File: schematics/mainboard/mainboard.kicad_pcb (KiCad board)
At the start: 4 copper layers, 99.5 x 193.5 mm, 94 parts, among them J1 SD_Card_Receptacle, J2 LCD_CONN, J3 USB_C_Receptacle_USB2.0_16P, J4 BATTERY_CONN, J5 527461671, J7 SPEAKER, J9 AudioJack3, P1 1-1473005-4, SW1 SW_SPST, U1 AMS1117-3.3, U2 AMS1117-3.3, U3 MAX3421EETJ_T, U5 AMS1117-1.8, U6 TPS63002, U7 BQ24072RGT, Y1 12MHz

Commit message: Added load switch to mainboard to control startup.
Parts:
- added C39: 47uF, Capacitor_SMD:CP_Elec_5x5.3, F.Cu at (125.8, 114.4)
- added C41: 200pF, Capacitor_SMD:C_0805_2012Metric, F.Cu at (152.2, 259.6)
- added R32: ~, Resistor_SMD:R_0603_1608Metric_Pad0.98x0.95mm_HandSolder, F.Cu at (152.2, 255.8)
- added U9: TPS22917DBV, Package_TO_SOT_SMD:SOT-23-6, F.Cu at (148.2, 257.6)
- moved C4 6.12 mm to (120.0, 112.8)
- moved R29 6.12 mm to (120.0, 115.3)
- moved R7 1.35 mm to (165.8, 268.9)
- moved R6 1.25 mm to (172.4, 268.9)
- moved R2 0.15 mm to (168.0, 268.9)
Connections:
- SW1 pad 2: SYS_LOAD -> Net-(SW1-B)
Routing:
- net Net-(J3-CC1): track 6.84 -> 5.31 mm
- net Net-(J3-CC2): track 6.64 -> 5.39 mm
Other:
- board text added: "3V3 (LCD, SD, AUDIO)"

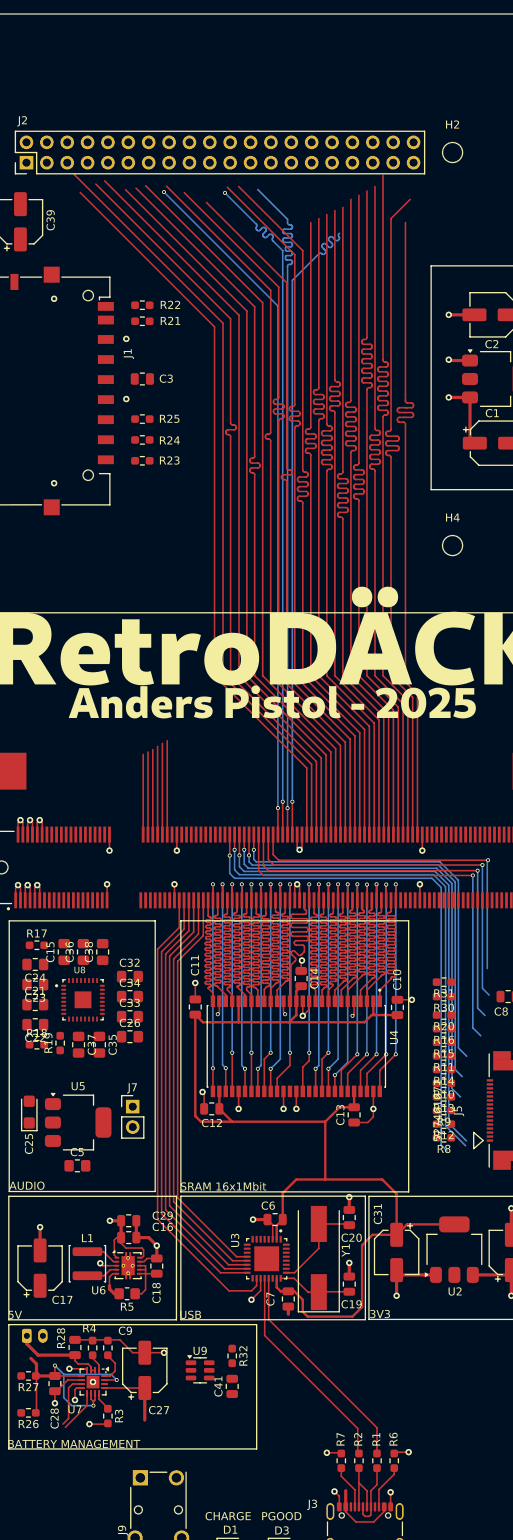
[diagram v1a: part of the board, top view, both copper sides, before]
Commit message: Mounting points for mainboard added. Adjusted position of track ball on buttboard.
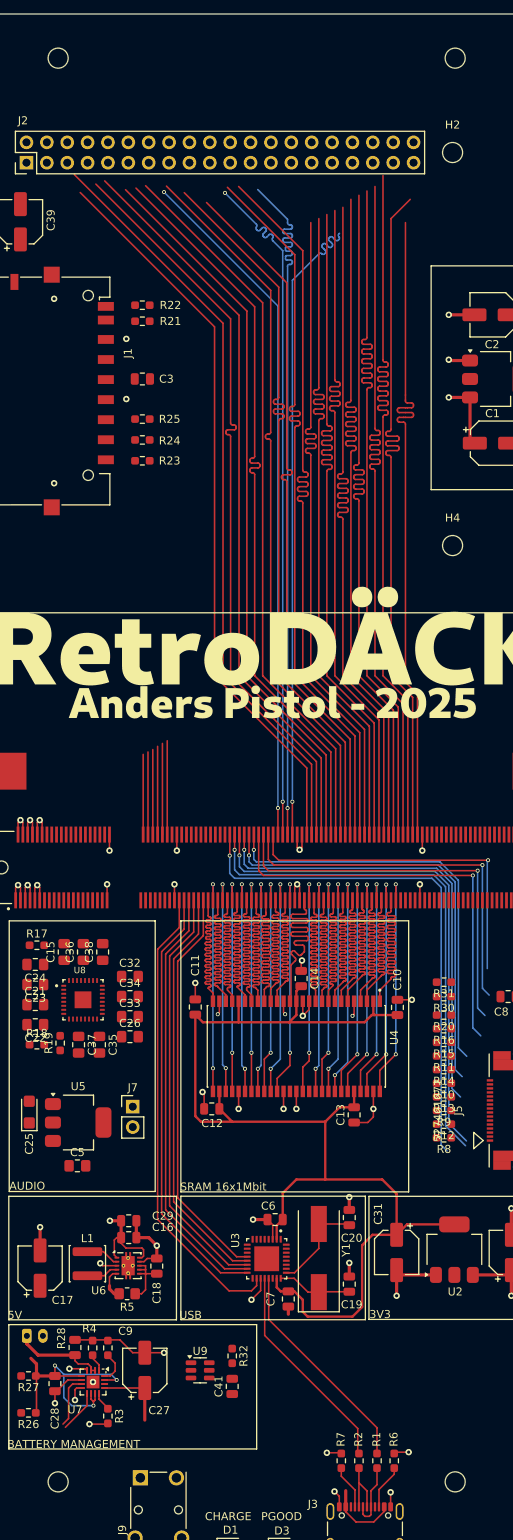
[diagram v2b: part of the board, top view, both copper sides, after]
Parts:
- added H5: MountingHole, MountingHole:MountingHole_2.5mm, F.Cu at (130.5, 94.0)
- added H6: MountingHole, MountingHole:MountingHole_2.5mm, F.Cu at (180.0, 94.0)
- added H7: MountingHole, MountingHole:MountingHole_2.5mm, F.Cu at (130.5, 271.5)
- added H8: MountingHole, MountingHole:MountingHole_2.5mm, F.Cu at (180.0, 271.5)

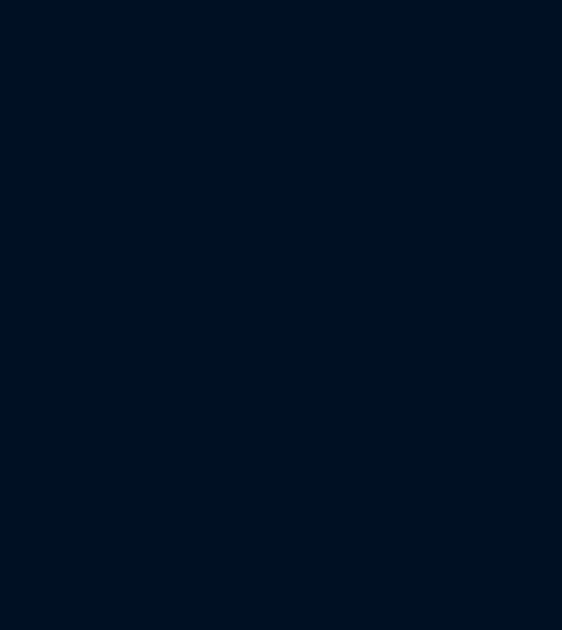
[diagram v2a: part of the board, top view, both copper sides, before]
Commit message: Schematic work; I2C shared with trackball and audio chip.
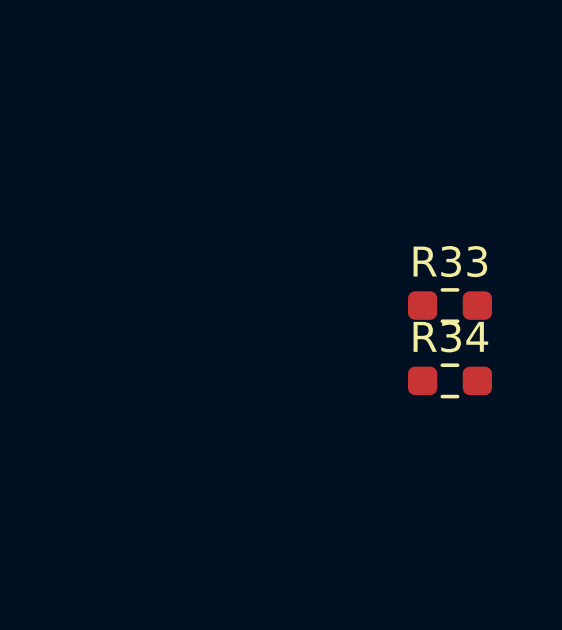
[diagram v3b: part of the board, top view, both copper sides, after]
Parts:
- added R33: 4k7, Resistor_SMD:R_0603_1608Metric_Pad0.98x0.95mm_HandSolder, F.Cu at (238.0, 211.5)
- added R34: 4k7, Resistor_SMD:R_0603_1608Metric_Pad0.98x0.95mm_HandSolder, F.Cu at (238.0, 214.0)
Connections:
- P1 pad 54: unconnected-(P1-Pad54) -> SD_CARD
- P1 pad 64: unconnected-(P1-Pad64) -> AUDIO_DIN
- P1 pad 66: unconnected-(P1-Pad66) -> AUDIO_WCLK
- P1 pad 68: unconnected-(P1-Pad68) -> AUDIO_BCLK
- P1 pad 70: unconnected-(P1-Pad70) -> AUDIO_MCLK
- U8 pad 10: AUDIO_SCL -> I2C_SCL
- U8 pad 9: AUDIO_SDA -> I2C_SDA

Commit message: Some work on the mainboard.
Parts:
- removed J7: SPEAKER, Connector_PinHeader_2.54mm:PinHeader_1x02_P2.54mm_Vertical
- removed R18, R19: 4k7, Resistor_SMD:R_0603_1608Metric_Pad0.98x0.95mm_HandSolder
- removed R30, R31: 1k2, Resistor_SMD:R_0603_1608Metric_Pad0.98x0.95mm_HandSolder
- added C40: 47uF, Capacitor_SMD:CP_Elec_5x5.3, F.Cu at (184.6, 118.9)
- added J6: SPEAKER_CONN, Connector_JST:JST_PH_S2B-PH-K_1x02_P2.00mm_Horizontal, F.Cu at (119.0, 224.0)
- moved C4 3.00 mm to (117.0, 112.8)
- moved C39 2.91 mm to (122.9, 114.2), turned to -90 degrees
- moved R29 2.12 mm to (118.0, 116.0), turned to 90 degrees
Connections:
- net I2C_INTERRUPT renamed TRACKBALL_INTERRUPT
- P1 pad 72: unconnected-(P1-Pad72) -> AUDIO_INTERRUPT
- U8 pad 32: GPIO1 -> AUDIO_INTERRUPT
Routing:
- net GND: track 146.2 -> 205.9 mm, vias 54 -> 55
- net 3V3_AUDIO: track 8.64 -> 67.5 mm
- net USB_VBUS: track 18.1 -> 47.5 mm
- net LCD_R4: track 88.1 -> 58.9 mm
- net LCD_B2: track 91.7 -> 71.8 mm
- net SD_CARD: track 0.00 -> 18.3 mm
- net LCD_B4: track 84.2 -> 71.5 mm
- net LCD_B3: track 85.6 -> 97.6 mm
- net LCD_ENABLE: track 86.3 -> 97.1 mm
- net 1V8: track 0.00 -> 8.72 mm
- net LCD_CLK: track 89.2 -> 97.5 mm
- net LCD_B1: track 89.8 -> 96.9 mm
- net LCD_G3: track 90.8 -> 97.6 mm
- net LCD_R5: track 91.4 -> 97.9 mm
- net LCD_CS: track 90.7 -> 97.0 mm
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
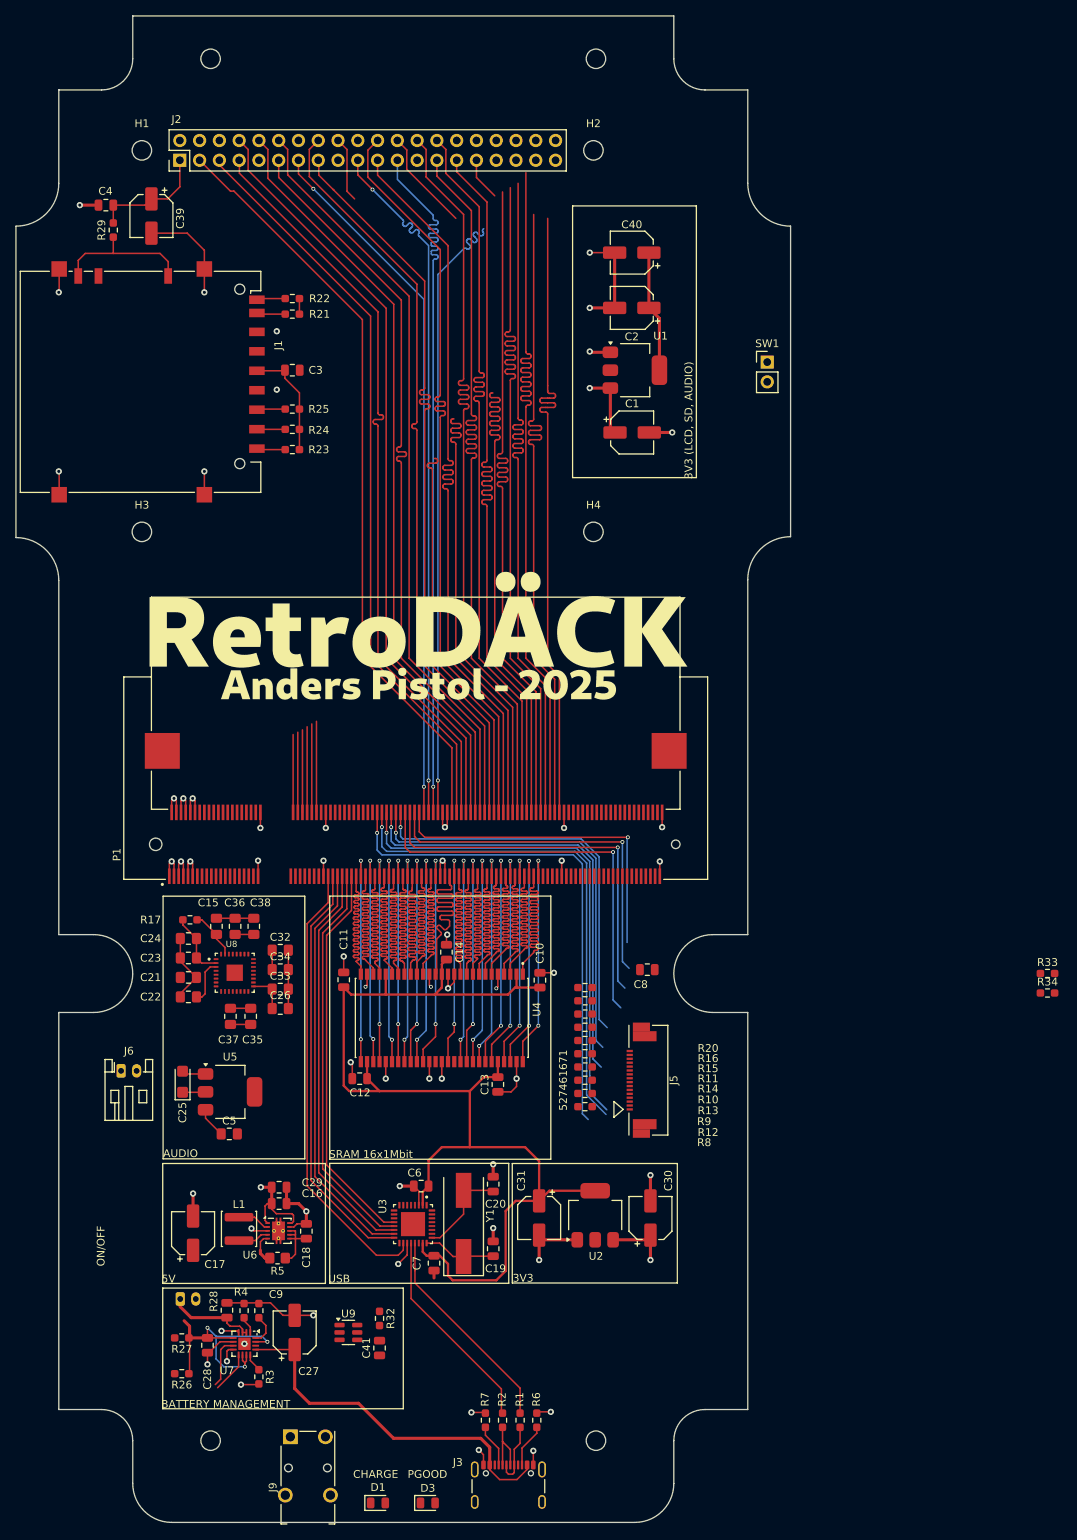
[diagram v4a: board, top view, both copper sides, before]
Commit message: Revision 1 of mainboard finished and ordered from JLCPCB.
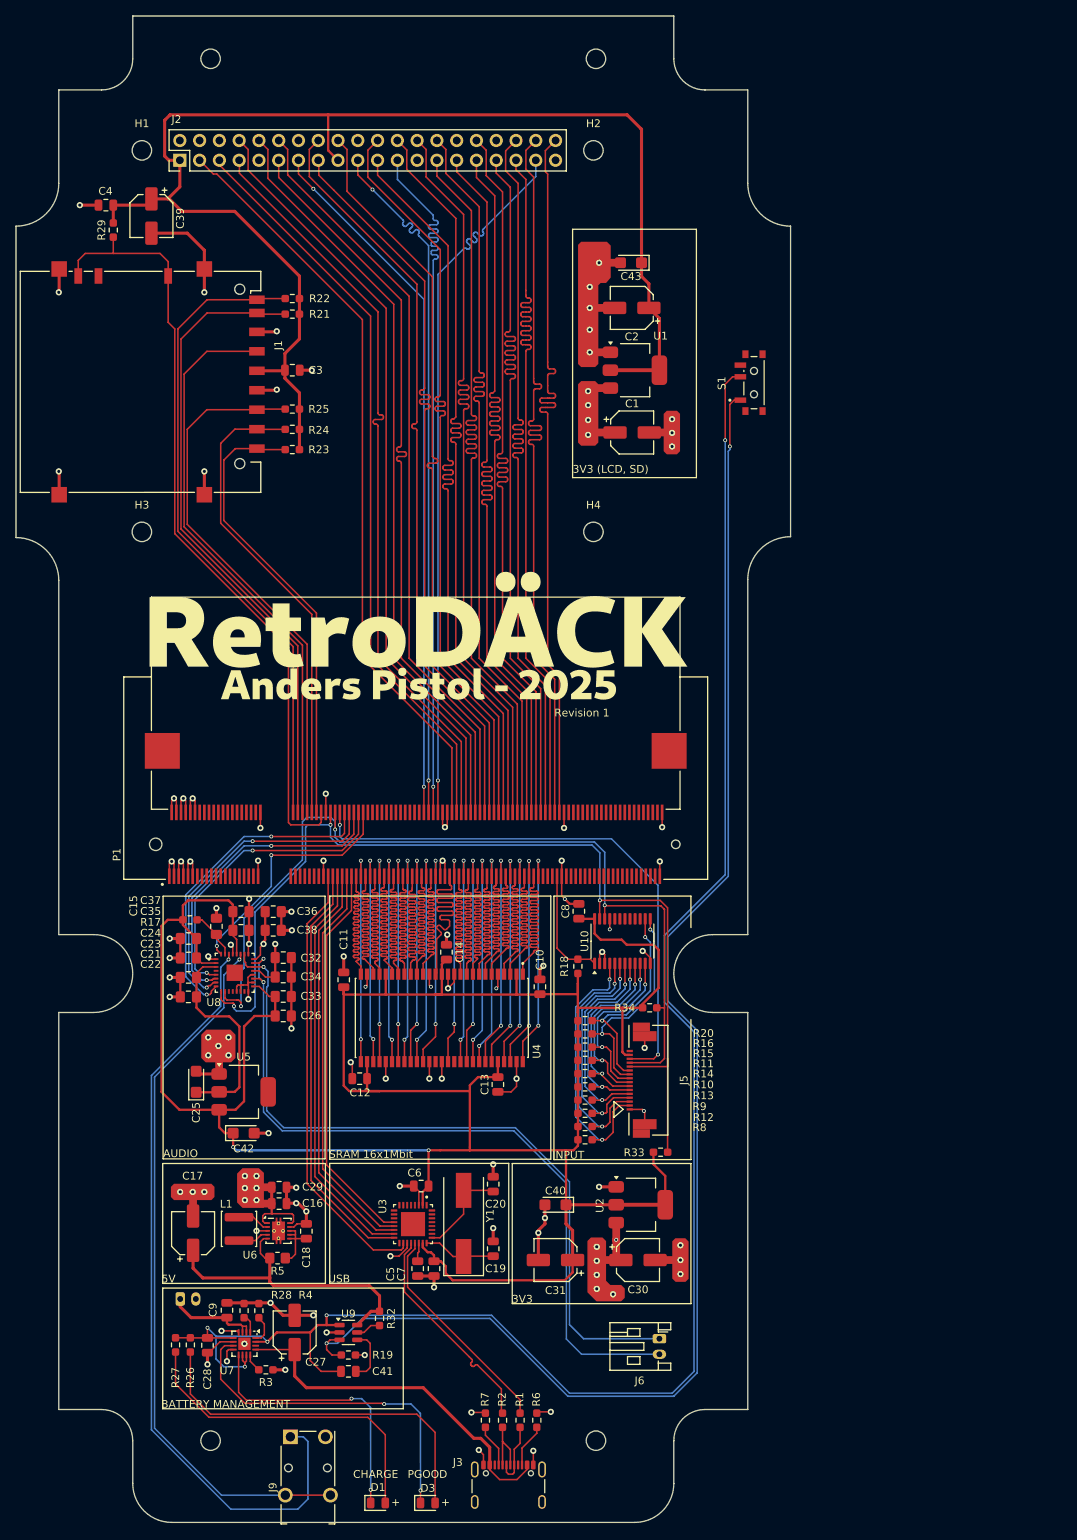
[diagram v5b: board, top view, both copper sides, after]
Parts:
- removed SW1: SW_SPST, Connector_PinHeader_2.54mm:PinHeader_1x02_P2.54mm_Vertical
- added C42: 10uF, Capacitor_Tantalum_SMD:CP_EIA-3216-18_Kemet-A, F.Cu at (134.7, 232.0)
- added C43: 47uF, Capacitor_Tantalum_SMD:CP_EIA-3216-18_Kemet-A, F.Cu at (184.5, 120.2)
- added R18: 10k, Resistor_SMD:R_0603_1608Metric_Pad0.98x0.95mm_HandSolder, F.Cu at (177.7, 210.6)
- added R19: 10k, Resistor_SMD:R_0603_1608Metric_Pad0.98x0.95mm_HandSolder, F.Cu at (148.2, 260.5)
- added S1: SSSS811101, SSSS811101:SW_SSSS811101, F.Cu at (200.3, 135.6)
- added U10: PCA9555PW, Package_SO:TSSOP-24_4.4x7.8mm_P0.65mm, F.Cu at (183.4, 207.3)
- C18: value 0.1u -> 0.1uF
- C40: footprint Capacitor_SMD:CP_Elec_5x5.3 -> Capacitor_Tantalum_SMD:CP_EIA-3216-18_Kemet-A
- C41: value 200pF -> 500pF
- C5: value 10uF -> 1uF; footprint Capacitor_SMD:C_0805_2012Metric_Pad1.18x1.45mm_HandSolder -> Capacitor_SMD:C_0805_2012Metric
- R26: value 1k -> 68
- R27: value 1k -> 30
- R29: value 57k -> 10k
- R3: value 1.18k -> 1.2k
- R32: value ~ -> NC
- R4: value 1.13k -> 1.2k
- moved C40 122.7 mm to (174.8, 241.2)
- moved J6 77.2 mm to (188.2, 258.4), turned to -90 degrees
- moved R33 54.7 mm to (188.3, 234.4)
- moved R34 51.1 mm to (186.9, 215.9)
- moved C5 29.7 mm to (157.1, 249.4), turned to 90 degrees
- moved C35 13.5 mm to (134.4, 203.6), turned to 0 degrees
- moved C8 11.6 mm to (177.8, 203.5), turned to -90 degrees
- moved C37 11.1 mm to (134.4, 205.9), turned to 0 degrees
- moved U2 6.00 mm to (185.8, 241.2), turned to 0 degrees
- moved C31 5.79 mm to (174.8, 248.3), turned to 180 degrees
- moved C30 5.63 mm to (185.4, 248.3), turned to 0 degrees
- moved C36 5.25 mm to (138.6, 203.6), turned to 0 degrees
- moved C41 5.00 mm to (148.2, 262.6), turned to 0 degrees
- moved R10 4.25 mm to (178.6, 226.1)
- moved R11 4.25 mm to (178.6, 222.7)
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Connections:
- C2 pad 1: 3V3_AUDIO -> 3V3_LCD
- C23 pad 1: 3V3_AUDIO -> 3V3
- C24 pad 1: 3V3_AUDIO -> 3V3
- C26 pad 1: 3V3_AUDIO -> 3V3
- C28 pad 2: Net-(SW1-A) -> Net-(U7-EN2)
- C3 pad 2: 3V3_AUDIO -> 3V3_LCD
- C33 pad 1: 3V3_AUDIO -> 3V3
- C35 pad 1: 3V3_AUDIO -> 3V3
- C37 pad 1: 3V3_AUDIO -> 3V3
- C39 pad 1: 3V3_AUDIO -> 3V3_LCD
- C4 pad 2: 3V3_AUDIO -> 3V3_LCD
- C40 pad 1: 3V3_AUDIO -> 3V3
- C41 pad 1: GND -> Net-(U7-EN2)
- C5 pad 1: 3V3_AUDIO -> GND
- C5 pad 2: GND -> Net-(U3-VBCOMP)
- J1 pad 4: 3V3_AUDIO -> 3V3_LCD
- J2 pad 1: 3V3_AUDIO -> 3V3_LCD
- J2 pad 17: 3V3_AUDIO -> 3V3_LCD
- J5 pad 10: HIO_BTN_X -> Net-(U10-IO1_0)
- J5 pad 11: HIO_BTN_RESET -> Net-(U10-IO1_1)
- J5 pad 15: unconnected-(J5-Pad15) -> 3V3
- J5 pad 2: HIO_DPAD_N -> Net-(U10-IO0_0)
- J5 pad 3: HIO_DPAD_S -> Net-(U10-IO0_1)
- J5 pad 4: HIO_DPAD_W -> Net-(U10-IO0_2)
- J5 pad 5: HIO_DPAD_E -> Net-(U10-IO0_3)
- J5 pad 6: HIO_BTN_A -> Net-(U10-IO0_4)
- J5 pad 7: HIO_BTN_B -> Net-(U10-IO0_5)
- J5 pad 8: HIO_BTN_C -> Net-(U10-IO0_6)
- J5 pad 9: HIO_BTN_D -> Net-(U10-IO0_7)
- J5 pad P1: unconnected-(J5-PadP1) -> GND
- J5 pad P2: 3V3 -> GND
- P1 pad 155: unconnected-(P1-Pad155) -> KEYPAD_INTERRUPT
- P1 pad 58: I2C_SCL -> I2C_SDA
- P1 pad 60: I2C_SDA -> I2C_SCL
- P1 pad 64: AUDIO_DIN -> AUDIO_MCLK
- P1 pad 66: AUDIO_WCLK -> AUDIO_BCLK
- P1 pad 68: AUDIO_BCLK -> AUDIO_WCLK
- P1 pad 70: AUDIO_MCLK -> AUDIO_DIN
- P1 pad 78: HIO_DPAD_N -> unconnected-(P1-Pad78)
- P1 pad 80: HIO_DPAD_S -> unconnected-(P1-Pad80)
- P1 pad 82: HIO_DPAD_W -> unconnected-(P1-Pad82)
- P1 pad 84: HIO_DPAD_E -> unconnected-(P1-Pad84)
- P1 pad 86: HIO_BTN_A -> unconnected-(P1-Pad86)
- P1 pad 88: HIO_BTN_B -> unconnected-(P1-Pad88)
- P1 pad 90: HIO_BTN_C -> unconnected-(P1-Pad90)
- P1 pad 92: HIO_BTN_D -> unconnected-(P1-Pad92)
- P1 pad 94: HIO_BTN_X -> unconnected-(P1-Pad94)
- P1 pad 96: HIO_BTN_RESET -> unconnected-(P1-Pad96)
- R10 pad 1: HIO_BTN_A -> Net-(U10-IO0_4)
- R11 pad 1: HIO_BTN_C -> Net-(U10-IO0_6)
- R12 pad 1: HIO_DPAD_S -> Net-(U10-IO0_1)
- R13 pad 1: HIO_DPAD_E -> Net-(U10-IO0_3)
- R14 pad 1: HIO_BTN_B -> Net-(U10-IO0_5)
- R15 pad 1: HIO_BTN_D -> Net-(U10-IO0_7)
- R16 pad 1: HIO_BTN_X -> Net-(U10-IO1_0)
- R17 pad 1: 3V3_AUDIO -> 3V3
- R20 pad 1: HIO_BTN_RESET -> Net-(U10-IO1_1)
- R21 pad 2: 3V3_AUDIO -> 3V3_LCD
- R22 pad 2: 3V3_AUDIO -> 3V3_LCD
- R23 pad 2: 3V3_AUDIO -> 3V3_LCD
- R24 pad 2: 3V3_AUDIO -> 3V3_LCD
- R25 pad 2: 3V3_AUDIO -> 3V3_LCD
- R26 pad 1: Net-(SW1-A) -> Net-(U7-EN2)
- R27 pad 1: Net-(SW1-A) -> Net-(U7-EN2)
- R29 pad 2: 3V3_AUDIO -> 3V3_LCD
- R33 pad 2: I2C_SCL -> I2C_SDA
- R34 pad 2: I2C_SDA -> I2C_SCL
- R8 pad 1: HIO_DPAD_N -> Net-(U10-IO0_0)
- R9 pad 1: HIO_DPAD_W -> Net-(U10-IO0_2)
- U1 pad 2: 3V3_AUDIO -> 3V3_LCD
- U3 pad 22: unconnected-(U3-VBCOMP-Pad22) -> Net-(U3-VBCOMP)
- U5 pad 3: 3V3_AUDIO -> 3V3
- U7 pad 10: Net-(SW1-A) -> Net-(U7-EN2)
- U7 pad 11: Net-(SW1-A) -> Net-(U7-EN2)
- U7 pad 15: Net-(SW1-A) -> Net-(U7-EN2)
- U7 pad 5: Net-(SW1-A) -> Net-(U7-EN2)
- U8 pad 11: VOL/MICDET -> unconnected-(U8-VOL/MICDET-Pad11)
- U8 pad 17: 3V3_AUDIO -> 3V3
- U8 pad 2: 3V3_AUDIO -> 3V3
- U8 pad 28: 3V3_AUDIO -> 3V3
- U9 pad 1: Net-(SW1-A) -> Net-(U7-EN2)
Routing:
- net Net-(U7-EN2): track 0.00 -> 234.4 mm, vias 0 -> 5
- net 3V3: track 144.3 -> 349.8 mm, vias 0 -> 2
- net Net-(U9-ON): track 0.00 -> 190.0 mm, vias 0 -> 2
- net 3V3_LCD: track 0.00 -> 177.3 mm
- net I2C_SDA: track 0.00 -> 129.0 mm, vias 0 -> 3
- net I2C_SCL: track 0.00 -> 116.1 mm, vias 0 -> 3
- net Net-(U8-HPR): track 0.00 -> 100.0 mm, vias 0 -> 1
- net Net-(J6-Pin_2): track 0.00 -> 98.6 mm, vias 0 -> 2
- net Net-(J6-Pin_1): track 0.00 -> 96.0 mm, vias 0 -> 1
- net Net-(U8-HPL): track 0.00 -> 91.6 mm, vias 0 -> 1
- net SD_CARD: track 18.3 -> 100.6 mm
- net TRACKBALL_INTERRUPT: track 0.00 -> 72.2 mm, vias 0 -> 2
- net SD_DAT1: track 13.7 -> 83.6 mm
- net SD_DAT0: track 14.0 -> 81.9 mm
- net 3V3_AUDIO: track 67.5 -> 0.00 mm
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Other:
- board text added: "+"
- board text added: "3V3 (LCD, SD)"
- board text added: "CHARGE - White LED PGOOD - Green LED"
- board text added: "INPUT"
- board text added: "Revision 1"
- board text removed: "3V3 (LCD, SD, AUDIO)"
- board text removed: "ON/OFF"
